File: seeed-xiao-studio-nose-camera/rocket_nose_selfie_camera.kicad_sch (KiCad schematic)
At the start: 20 parts, among them J1 LOGGER TRIGGER / STATUS, J2 UART DEBUG (3V3 TTL), J3 LOGGER CAN, U1 Seeed Studio XIAO ESP32-S3 Se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, U2 SN65HVD230DR

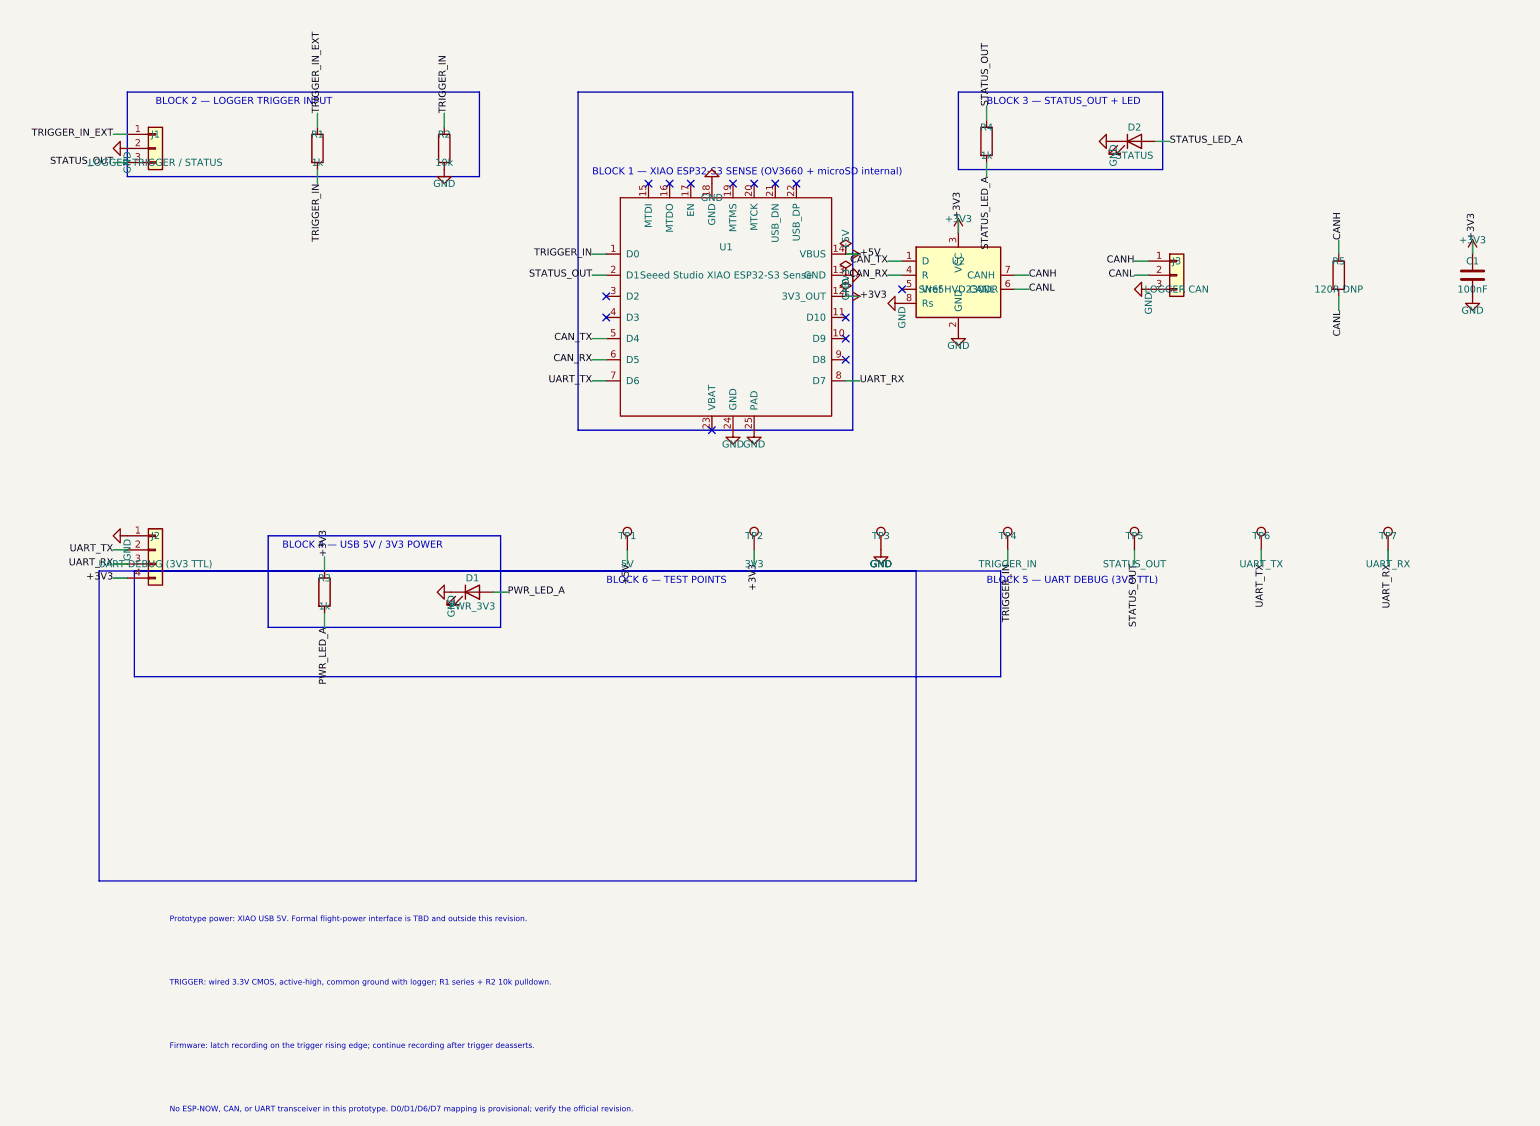
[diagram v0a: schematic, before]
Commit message: sch: complete schematic presentation
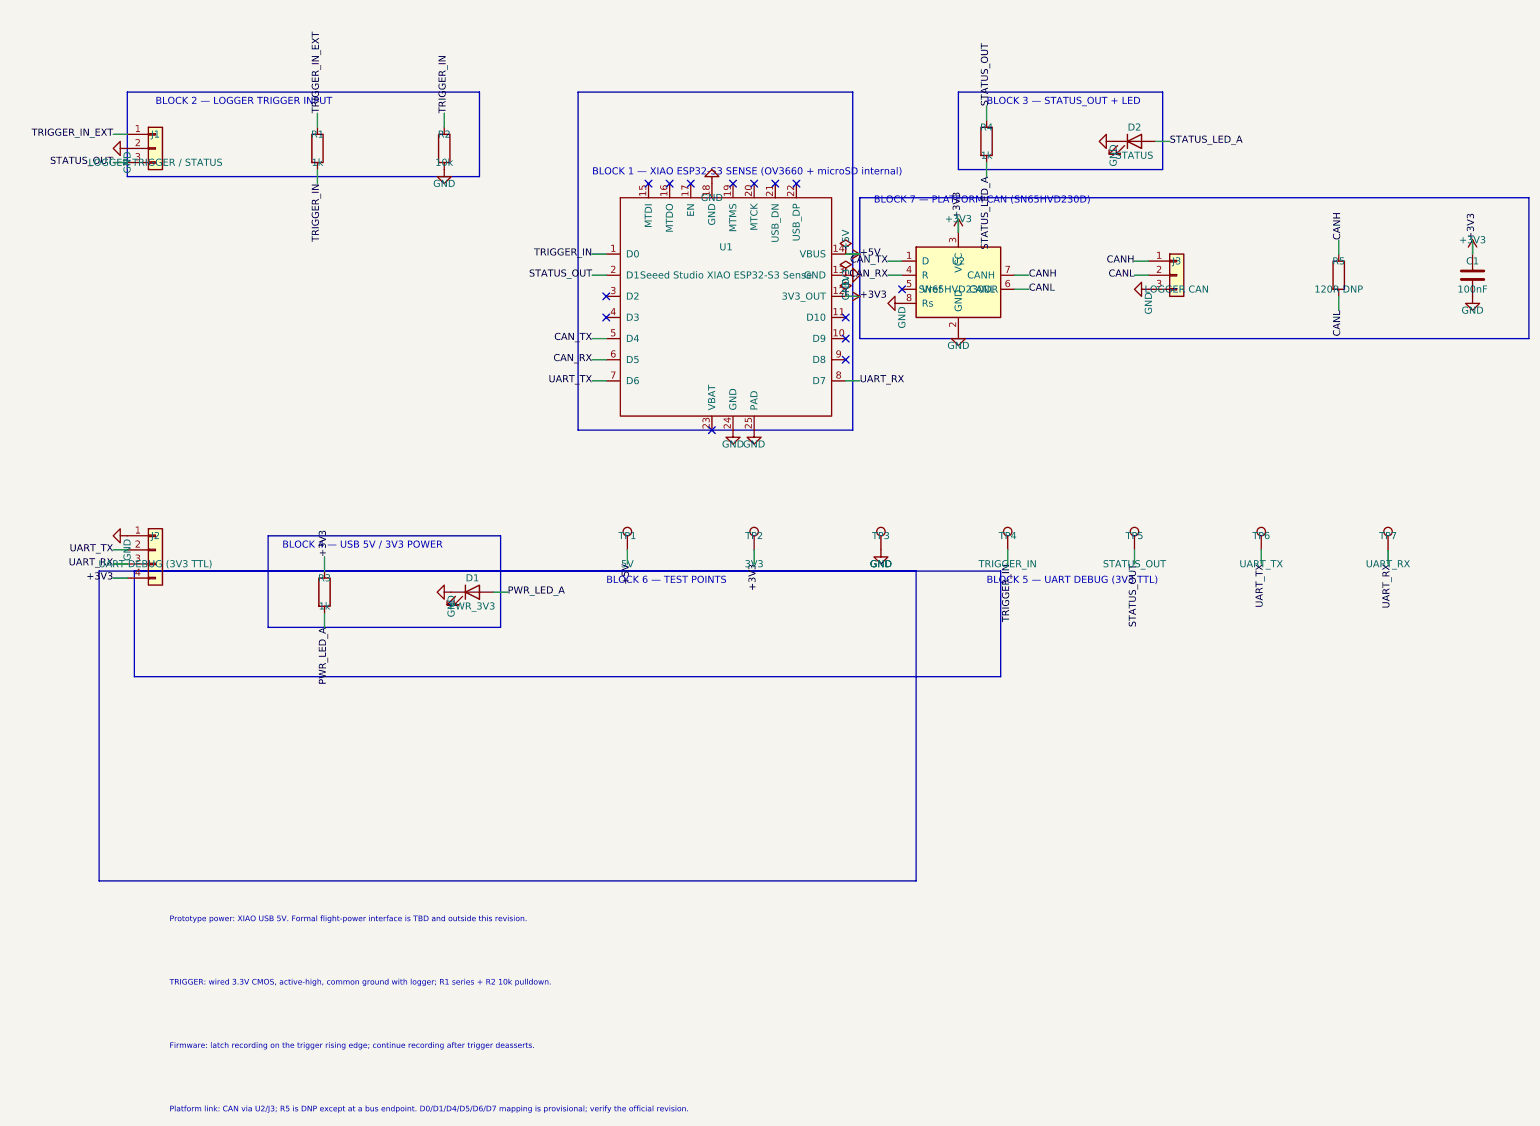
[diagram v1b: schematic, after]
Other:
- note added: "BLOCK 7 — PLATFORM CAN (SN65HVD230D)"
- note added: "Platform link: CAN via U2/J3; R5 is DNP except at a bus endpoint. D0/D1/D4/D5/D6/D7 mapping is provisional; verify the official revision."
- note removed: "No ESP-NOW, CAN, or UART transceiver in this prototype. D0/D1/D6/D7 mapping is provisional; verify the official revision."
